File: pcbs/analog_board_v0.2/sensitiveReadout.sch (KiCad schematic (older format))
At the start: 28 parts, among them J4 CONN_01X01, U2 ADA4522-2

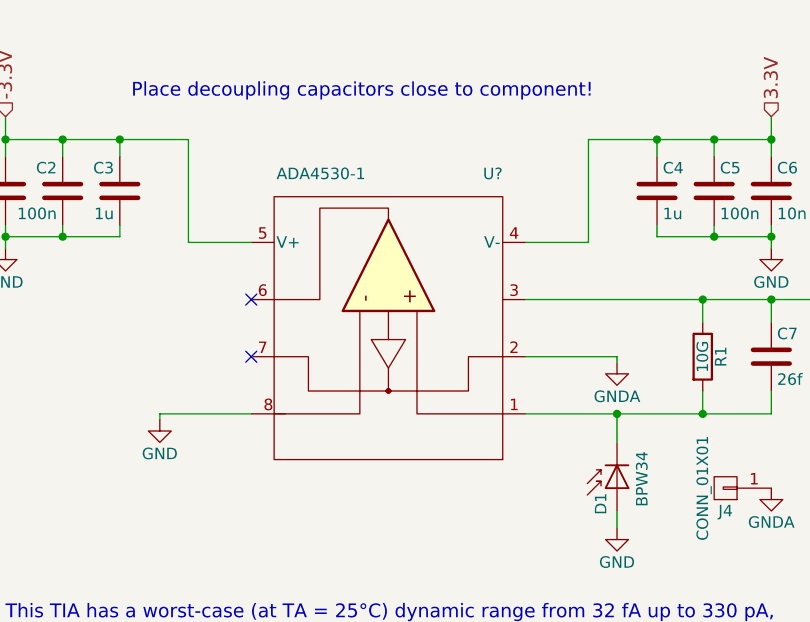
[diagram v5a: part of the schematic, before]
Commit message: Finished the photo extender, backplane and the analog board.
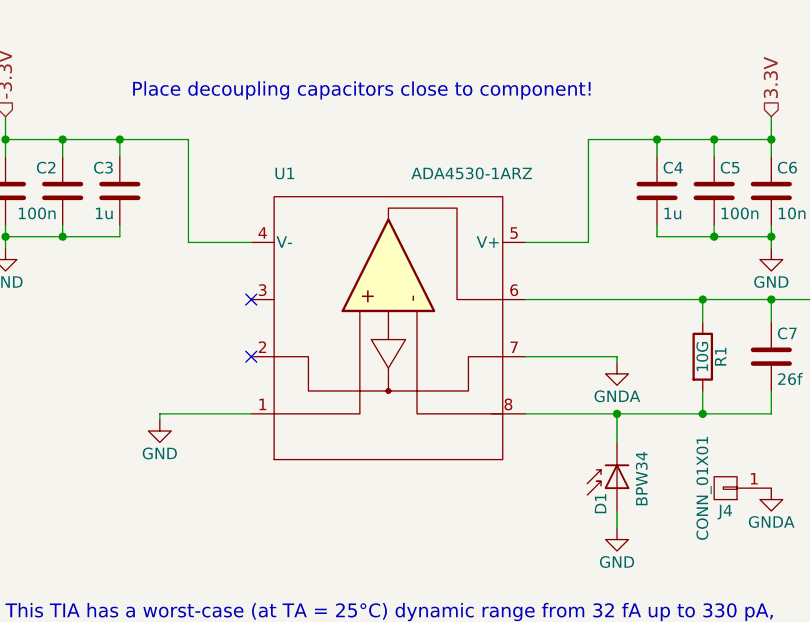
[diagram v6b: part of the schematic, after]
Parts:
- U1: renamed from U?; value ADA4530-1 -> ADA4530-1ARZ; footprint (none) -> SMD_Packages:SOIC-8-N; Farnell (none) -> 2521248
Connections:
- net -3.3V: now also U1.4 (V-); no longer U1.5 (V+)
- net 3.3V: now also U1.5 (V+); no longer U1.4 (V-)
- net GND: now also U1.1; no longer U1.8
- net GNDA: now also U1.7; no longer U1.2
- net at C7.2, D1.1 (K), R1.2: now also U1.8; no longer U1.1
- net at C7.1, R1.1, R2.1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: now also U1.6; no longer U1.3
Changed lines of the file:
@@
 Sheet 2 4
 Title "Sensitive Measurement Part of Analog Board"
-Date "2017-06-14"
+Date "2017-07-05"
 Rev "v0.2"
-Comp ""
+Comp "UppSense Heart Failure Diagnostics"
 Comment1 ""
 Comment2 ""
@@
 $EndComp
 $Comp
-L GND #PWR05
+L GND #PWR8
 U 1 1 5940C884
 P 4750 5225
-F 0 "#PWR05" H 4750 4975 50  0001 C CNN
+F 0 "#PWR8" H 4750 4975 50  0001 C CNN
 F 1 "GND" H 4750 5075 50  0000 C CNN
 F 2 "" H 4750 5225 50  0000 C CNN
@@
 $EndComp
 $Comp
-L GND #PWR06
+L GND #PWR9
 U 1 1 5941B3F1
 P 5425 4000
-F 0 "#PWR06" H 5425 3750 50  0001 C CNN
+F 0 "#PWR9" H 5425 3750 50  0001 C CNN
 F 1 "GND" H 5425 3850 50  0000 C CNN
 F 2 "" H 5425 4000 50  0000 C CNN
@@
 $EndComp
 $Comp
-L GND #PWR07
+L GND #PWR5
 U 1 1 5957E72A
 P 2075 4000
-F 0 "#PWR07" H 2075 3750 50  0001 C CNN
+F 0 "#PWR5" H 2075 3750 50  0001 C CNN
 F 1 "GND" H 2075 3850 50  0000 C CNN
 F 2 "" H 2075 4000 50  0000 C CNN
@@
 $EndComp
 $Comp
-L GND #PWR08
+L GND #PWR6
 U 1 1 5957EBB0
 P 2750 4750
-F 0 "#PWR08" H 2750 4500 50  0001 C CNN
+F 0 "#PWR6" H 2750 4500 50  0001 C CNN
 F 1 "GND" H 2750 4600 50  0000 C CNN
 F 2 "" H 2750 4750 50  0000 C CNN
@@
 $EndComp
 $Comp
-L GND #PWR09
+L GND #PWR11
 U 1 1 59581E5E
 P 6150 3850
-F 0 "#PWR09" H 6150 3600 50  0001 C CNN
+F 0 "#PWR11" H 6150 3600 50  0001 C CNN
 F 1 "GND" H 6150 3700 50  0000 C CNN
 F 2 "" H 6150 3850 50  0000 C CNN
@@
 $EndComp
 $Comp
-L GND #PWR010
+L GND #PWR17
 U 1 1 59582484
 P 9850 3850
-F 0 "#PWR010" H 9850 3600 50  0001 C CNN
+F 0 "#PWR17" H 9850 3600 50  0001 C CNN
 F 1 "GND" H 9850 3700 50  0000 C CNN
 F 2 "" H 9850 3850 50  0000 C CNN
@@
 $EndComp
 $Comp
-L GND #PWR011
+L GND #PWR14
 U 1 1 595855AC
 P 7375 5200
-F 0 "#PWR011" H 7375 4950 50  0001 C CNN
+F 0 "#PWR14" H 7375 4950 50  0001 C CNN
 F 1 "GND" H 7375 5050 50  0000 C CNN
 F 2 "" H 7375 5200 50  0000 C CNN
@@
 $EndComp
 $Comp
-L GND #PWR012
+L GND #PWR13
 U 1 1 595860BB
 P 7375 3475
-F 0 "#PWR012" H 7375 3225 50  0001 C CNN
+F 0 "#PWR13" H 7375 3225 50  0001 C CNN
 F 1 "GND" H 7375 3325 50  0000 C CNN
 F 2 "" H 7375 3475 50  0000 C CNN
@@
 $EndComp
 $Comp
-L GND #PWR013
+L GND #PWR12
 U 1 1 5958CBA1
 P 6300 2625
-F 0 "#PWR013" H 6300 2375 50  0001 C CNN
+F 0 "#PWR12" H 6300 2375 50  0001 C CNN
 F 1 "GND" H 6300 2475 50  0000 C CNN
 F 2 "" H 6300 2625 50  0000 C CNN
@@
 $EndComp
 $Comp
-L GND #PWR014
+L GND #PWR15
 U 1 1 5958D9EA
 P 7625 2625
-F 0 "#PWR014" H 7625 2375 50  0001 C CNN
+F 0 "#PWR15" H 7625 2375 50  0001 C CNN
 F 1 "GND" H 7625 2475 50  0000 C CNN
 F 2 "" H 7625 2625 50  0000 C CNN
@@
 $EndComp
 $Comp
-L GND #PWR015
+L GND #PWR16
 U 1 1 5958E51E
 P 9325 2625
-F 0 "#PWR015" H 9325 2375 50  0001 C CNN
+F 0 "#PWR16" H 9325 2375 50  0001 C CNN
 F 1 "GND" H 9325 2475 50  0000 C CNN
 F 2 "" H 9325 2625 50  0000 C CNN
@@
 RC filters have a cut-off frequency of approx. 663 Hz.
 $Comp
-L GNDA #PWR016
+L GNDA #PWR7
 U 1 1 59590E1C
 P 4750 4500
-F 0 "#PWR016" H 4750 4250 50  0001 C CNN
+F 0 "#PWR7" H 4750 4250 50  0001 C CNN
 F 1 "GNDA" H 4750 4350 50  0000 C CNN
 F 2 "" H 4750 4500 50  0001 C CNN
@@
 $EndComp
 $Comp
-L GNDA #PWR017
+L GNDA #PWR10
 U 1 1 595A3A5F
 P 5425 5050
-F 0 "#PWR017" H 5425 4800 50  0001 C CNN
+F 0 "#PWR10" H 5425 4800 50  0001 C CNN
 F 1 "GNDA" H 5425 4900 50  0000 C CNN
 F 2 "" H 5425 5050 50  0001 C CNN
@@
 $EndComp
 $Comp
-L ADA4530-1 U?
+L ADA4530-1 U1
 U 1 1 595C1871
 P 3750 4525
-F 0 "U?" H 3250 3675 50  0000 L CNN
-F 1 "ADA4530-1" H 3850 3675 50  0000 L CNN
-F 2 "" V 3800 3972 50  0000 C CNN
-F 3 "" V 3900 4022 50  0000 C CNN
+F 0 "U1" H 3250 3675 50  0000 L CNN
+F 1 "ADA4530-1ARZ" H 3850 3675 50  0000 L CNN
+F 2 "SMD_Packages:SOIC-8-N" V 3800 3972 50  0001 C CNN
+F 3 "http://www.analog.com/media/en/technical-documentation/data-sheets/ADA4530-1.pdf" V 3900 4022 50  0001 C CNN
+F 4 "2521248" H 3750 4525 60  0001 C CNN "Farnell"
 	1    3750 4525
-	-1   0    0    1
+	1    0    0    1
 $EndComp
 $EndSCHEMATC

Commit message: Added BOMs and gerber files.
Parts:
- C16: Farnell 499687 -> 2502703
- R1: Farnell 2420577 -> 2420567
- R2, R5, R6: Farnell WR08X2401FTL -> 2502703
- U2: value ADA4522-2 -> ADA4522-2ARZ; Farnell ADA4522-2ARZ -> 2505560
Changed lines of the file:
@@
 $EndComp
 $Comp
-L GND #PWR8
+L GND #PWR05
 U 1 1 5940C884
 P 4750 5225
-F 0 "#PWR8" H 4750 4975 50  0001 C CNN
+F 0 "#PWR05" H 4750 4975 50  0001 C CNN
 F 1 "GND" H 4750 5075 50  0000 C CNN
 F 2 "" H 4750 5225 50  0000 C CNN
@@
 $EndComp
 $Comp
-L GND #PWR9
+L GND #PWR06
 U 1 1 5941B3F1
 P 5425 4000
-F 0 "#PWR9" H 5425 3750 50  0001 C CNN
+F 0 "#PWR06" H 5425 3750 50  0001 C CNN
 F 1 "GND" H 5425 3850 50  0000 C CNN
 F 2 "" H 5425 4000 50  0000 C CNN
@@
 F 2 "WithoutSilkscreen:R_0805_W_Silks" V 5055 4475 50  0001 C CNN
 F 3 "http://www.farnell.com/datasheets/1928778.pdf" H 5125 4475 50  0001 C CNN
-F 4 "2420577" V 5125 4475 60  0001 C CNN "Farnell"
+F 4 "2420567" V 5125 4475 60  0001 C CNN "Farnell"
 	1    5125 4475
 	1    0    0    -1
@@
 $EndComp
 $Comp
-L GND #PWR5
+L GND #PWR07
 U 1 1 5957E72A
 P 2075 4000
-F 0 "#PWR5" H 2075 3750 50  0001 C CNN
+F 0 "#PWR07" H 2075 3750 50  0001 C CNN
 F 1 "GND" H 2075 3850 50  0000 C CNN
 F 2 "" H 2075 4000 50  0000 C CNN
@@
 $EndComp
 $Comp
-L GND #PWR6
+L GND #PWR08
 U 1 1 5957EBB0
 P 2750 4750
-F 0 "#PWR6" H 2750 4500 50  0001 C CNN
+F 0 "#PWR08" H 2750 4500 50  0001 C CNN
 F 1 "GND" H 2750 4600 50  0000 C CNN
 F 2 "" H 2750 4750 50  0000 C CNN
@@
 P 8025 4125
 F 0 "U2" H 7404 3829 50  0000 L CNN
-F 1 "ADA4522-2" H 8225 3825 50  0000 L CNN
+F 1 "ADA4522-2ARZ" H 8075 3825 50  0000 L CNN
 F 2 "SMD_Packages:SOIC-8-N" H 7828 4175 50  0001 C CNN
 F 3 "http://www.farnell.com/datasheets/2171839.pdf" H 7728 4275 50  0001 C CNN
-F 4 "ADA4522-2ARZ" H 8025 4125 60  0001 C CNN "Farnell"
+F 4 "2505560" H 8025 4125 60  0001 C CNN "Farnell"
 	1    8025 4125
 	1    0    0    -1
@@
 $EndComp
 $Comp
-L GND #PWR11
+L GND #PWR09
 U 1 1 59581E5E
 P 6150 3850
-F 0 "#PWR11" H 6150 3600 50  0001 C CNN
+F 0 "#PWR09" H 6150 3600 50  0001 C CNN
 F 1 "GND" H 6150 3700 50  0000 C CNN
 F 2 "" H 6150 3850 50  0000 C CNN
@@
 $EndComp
 $Comp
-L GND #PWR17
+L GND #PWR010
 U 1 1 59582484
 P 9850 3850
-F 0 "#PWR17" H 9850 3600 50  0001 C CNN
+F 0 "#PWR010" H 9850 3600 50  0001 C CNN
 F 1 "GND" H 9850 3700 50  0000 C CNN
 F 2 "" H 9850 3850 50  0000 C CNN
@@
 $EndComp
 $Comp
-L GND #PWR14
+L GND #PWR011
 U 1 1 595855AC
 P 7375 5200
-F 0 "#PWR14" H 7375 4950 50  0001 C CNN
+F 0 "#PWR011" H 7375 4950 50  0001 C CNN
 F 1 "GND" H 7375 5050 50  0000 C CNN
 F 2 "" H 7375 5200 50  0000 C CNN
@@
 $EndComp
 $Comp
-L GND #PWR13
+L GND #PWR012
 U 1 1 595860BB
 P 7375 3475
-F 0 "#PWR13" H 7375 3225 50  0001 C CNN
+F 0 "#PWR012" H 7375 3225 50  0001 C CNN
 F 1 "GND" H 7375 3325 50  0000 C CNN
 F 2 "" H 7375 3475 50  0000 C CNN
@@
 F 2 "Resistors_SMD:R_0805" V 5980 2200 50  0001 C CNN
 F 3 "" H 6050 2200 50  0001 C CNN
-F 4 "WR08X2401FTL" V 6050 2200 60  0001 C CNN "Farnell"
+F 4 "2502703" V 6050 2200 60  0001 C CNN "Farnell"
 	1    6050 2200
 	0    -1   -1   0
 $EndComp
 $Comp
-L GND #PWR12
+L GND #PWR013
 U 1 1 5958CBA1
 P 6300 2625
-F 0 "#PWR12" H 6300 2375 50  0001 C CNN
+F 0 "#PWR013" H 6300 2375 50  0001 C CNN
 F 1 "GND" H 6300 2475 50  0000 C CNN
 F 2 "" H 6300 2625 50  0000 C CNN
@@
 F 2 "Resistors_SMD:R_0805" V 7305 2200 50  0001 C CNN
 F 3 "" H 7375 2200 50  0001 C CNN
-F 4 "WR08X2401FTL" V 7375 2200 60  0001 C CNN "Farnell"
+F 4 "2502703" V 7375 2200 60  0001 C CNN "Farnell"
 	1    7375 2200
 	0    -1   -1   0
 $EndComp
 $Comp
-L GND #PWR15
+L GND #PWR014
 U 1 1 5958D9EA
 P 7625 2625
-F 0 "#PWR15" H 7625 2375 50  0001 C CNN
+F 0 "#PWR014" H 7625 2375 50  0001 C CNN
 F 1 "GND" H 7625 2475 50  0000 C CNN
 F 2 "" H 7625 2625 50  0000 C CNN
@@
 F 2 "Resistors_SMD:R_0805" H 9363 2275 50  0001 C CNN
 F 3 "" H 9325 2425 50  0000 C CNN
-F 4 "499687" H 9325 2425 60  0001 C CNN "Farnell"
+F 4 "2502703" H 9325 2425 60  0001 C CNN "Farnell"
 	1    9325 2425
 	-1   0    0    1
@@
 F 2 "Resistors_SMD:R_0805" V 9005 2200 50  0001 C CNN
 F 3 "" H 9075 2200 50  0001 C CNN
-F 4 "WR08X2401FTL" V 9075 2200 60  0001 C CNN "Farnell"
+F 4 "2502703" V 9075 2200 60  0001 C CNN "Farnell"
 	1    9075 2200
 	0    -1   -1   0
 $EndComp
 $Comp
-L GND #PWR16
+L GND #PWR015
 U 1 1 5958E51E
 P 9325 2625
-F 0 "#PWR16" H 9325 2375 50  0001 C CNN
+F 0 "#PWR015" H 9325 2375 50  0001 C CNN
 F 1 "GND" H 9325 2475 50  0000 C CNN
 F 2 "" H 9325 2625 50  0000 C CNN
@@
 RC filters have a cut-off frequency of approx. 663 Hz.
 $Comp
-L GNDA #PWR7
+L GNDA #PWR016
 U 1 1 59590E1C
 P 4750 4500
-F 0 "#PWR7" H 4750 4250 50  0001 C CNN
+F 0 "#PWR016" H 4750 4250 50  0001 C CNN
 F 1 "GNDA" H 4750 4350 50  0000 C CNN
 F 2 "" H 4750 4500 50  0001 C CNN
@@
 $EndComp
 $Comp
-L GNDA #PWR10
+L GNDA #PWR017
 U 1 1 595A3A5F
 P 5425 5050
-F 0 "#PWR10" H 5425 4800 50  0001 C CNN
+F 0 "#PWR017" H 5425 4800 50  0001 C CNN
 F 1 "GNDA" H 5425 4900 50  0000 C CNN
 F 2 "" H 5425 5050 50  0001 C CNN
